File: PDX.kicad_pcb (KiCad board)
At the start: 2 copper layers, 97.3 x 97 mm, 104 parts, among them Q1 BS170, Q2 BS170, Q3 BS170, Q4 BS170, Q5 BC547, Q6 BC547, U1 CD2003GB_GP, U2 SI5351_Module, U3 74ACT244, U6 LM393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

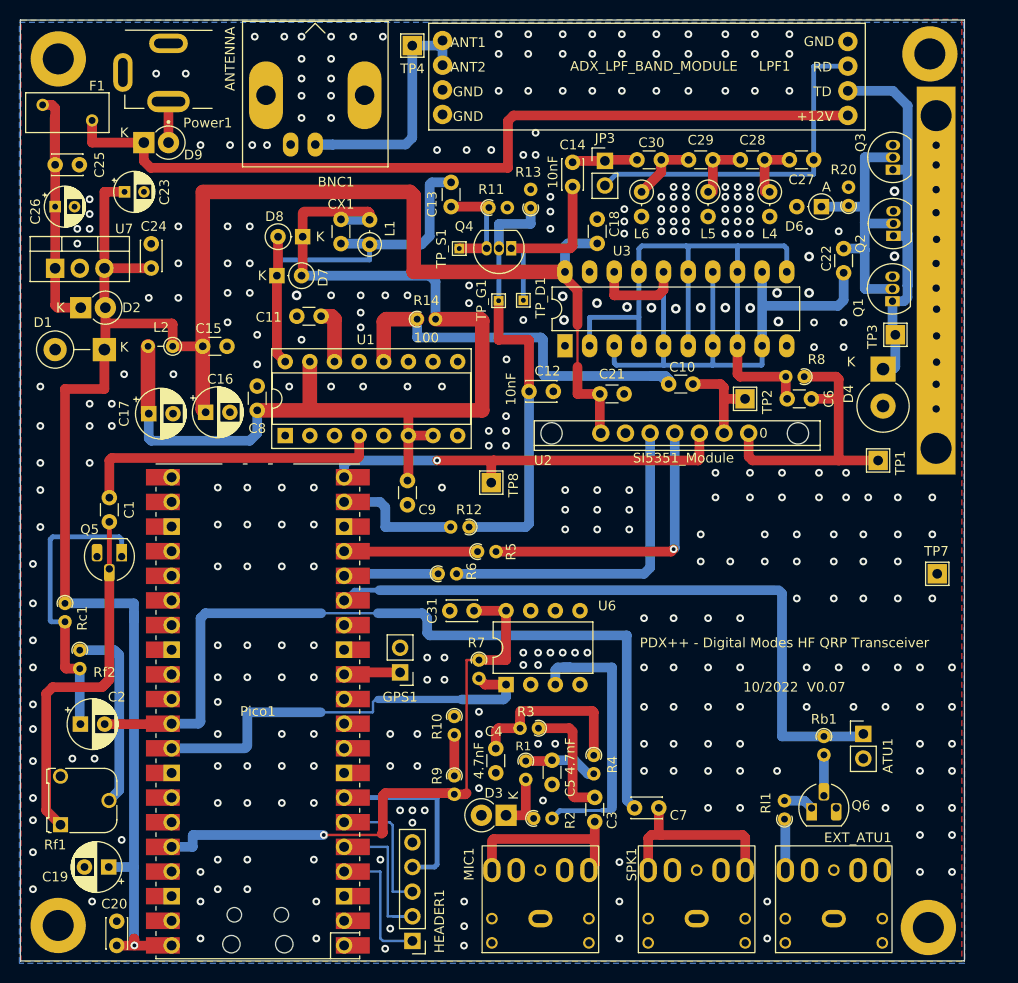
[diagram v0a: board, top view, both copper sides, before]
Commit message: PCB v0.2 + Initial firmware
PCB changes:

- Use `TO-92_HandSolder` footprint

- Use (optional) sockets for BS170 finals!

- Add `Test Point` for comparator output

- Remove onboard heatsink - it is not needed

- Provide +5V on the output header

- Make the +5V supply to Pico optional via a jumper

  - This enables external CAT control of Pico via USB

- Tie the unused LM393 inputs to ground

- Dual-input (+5V directly at VSYS and +5V from USB) power supply
  mechanism for Pico (similar to what Arduino Nano has).

Code changes:

- Initial firmware with CAT support (WSJT-X / 'FT8 Radio' Android app)

- The `freqPIO` stuff will be enabled later after testing
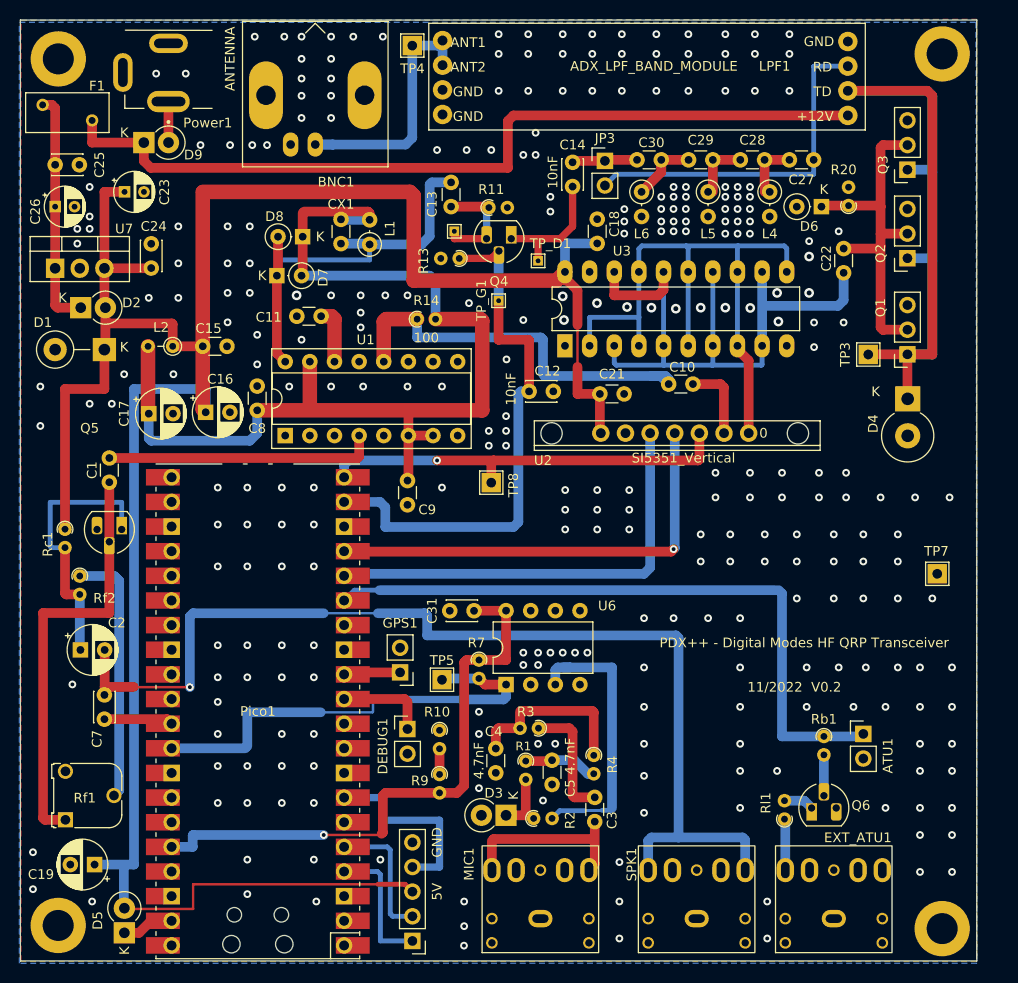
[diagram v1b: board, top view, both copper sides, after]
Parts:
- removed C20: 100nF, Capacitor_THT:C_Disc_D3.0mm_W2.0mm_P2.50mm
- removed C6: 100pF, Capacitor_THT:C_Disc_D3.0mm_W1.6mm_P2.50mm
- removed HS1: Heatsink_Pad, footprints:ThermalPad_Final
- removed R12, R5, R6: 330, Resistor_THT:R_Axial_DIN0204_L3.6mm_D1.6mm_P1.90mm_Vertical
- removed R8: 100, Resistor_THT:R_Axial_DIN0204_L3.6mm_D1.6mm_P1.90mm_Vertical
- removed TP1: CLK0, TestPoint:TestPoint_THTPad_2.0x2.0mm_Drill1.0mm
- removed TP2: CLK1, TestPoint:TestPoint_THTPad_2.0x2.0mm_Drill1.0mm
- added D5: 1N5818, Diode_THT:D_DO-41_SOD81_P2.54mm_Vertical_KathodeUp, F.Cu at (69.6, 106.9)
- added DEBUG1: Conn_01x02, Connector_PinHeader_2.54mm:PinHeader_1x02_P2.54mm_Vertical, F.Cu at (98.8, 85.9)
- added TP5: COUT, TestPoint:TestPoint_THTPad_2.0x2.0mm_Drill1.0mm, F.Cu at (102.4, 80.8)
- C26: value 100uF/16V -> 100uF/25V
- D6: footprint Diode_THT:D_DO-35_SOD27_P2.54mm_Vertical_AnodeUp -> Diode_THT:D_DO-35_SOD27_P2.54mm_Vertical_KathodeUp
- Q1, Q2, Q3: footprint Package_TO_SOT_THT:TO-92_Inline -> Connector_PinSocket_2.54mm:PinSocket_1x03_P2.54mm_Vertical
- Q4: footprint Package_TO_SOT_THT:TO-92_Inline -> Package_TO_SOT_THT:TO-92_HandSolder
- R20: value 2.7k -> 2.2k
- U2: value SI5351_Module -> SI5351_Vertical
- moved C7 57.9 mm to (67.6, 84.8), turned to 90 degrees
- moved R13 9.02 mm to (104.1, 37.3), turned to 180 degrees
- moved Rf2 7.65 mm to (65.0, 70.1)
- moved C2 7.64 mm to (65.1, 77.7)
- moved Rc1 7.64 mm to (63.5, 65.3)
- moved Q1 5.69 mm to (150.3, 47.2), turned to 180 degrees
- moved TP_D1 4.34 mm to (112.3, 37.6)
- moved C1 4.08 mm to (68.1, 57.9)
- moved D4 3.98 mm to (150.4, 51.8)
- moved TP3 3.45 mm to (146.3, 47.2)
- moved Q5 2.79 mm to (69.3, 65.3)
- moved Q2 2.73 mm to (150.3, 37.3), turned to 180 degrees
- moved R10 2.09 mm to (102.1, 86.0)
- moved TP_S1 1.85 mm to (103.6, 34.5), turned to 0 degrees
- moved R9 1.53 mm to (102.1, 90.5)
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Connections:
- C2 pad 2: TO_ADC -> Net-(C2-Pad2)
- C7 pad 1: Net-(C7-Pad1) -> TO_ADC
- C7 pad 2: TO_ADC -> Net-(C2-Pad2)
- HEADER1 pad 3: SW3 -> +5V
- Pico1 pad 11: unconnected-(Pico1-Pad11) -> Net-(DEBUG1-Pad1)
- Pico1 pad 19: Net-(Pico1-Pad19) -> RXSW
- Pico1 pad 39: unconnected-(Pico1-Pad39) -> Net-(D5-Pad1)
- Pico1 pad 40: +5V -> unconnected-(Pico1-Pad40)
- Pico1 pad 6: SW3 -> unconnected-(Pico1-Pad6)
- SPK1 pad R: Net-(C7-Pad1) -> Net-(C2-Pad2)
- SPK1 pad T: Net-(C7-Pad1) -> Net-(C2-Pad2)
- U2 pad 3: Net-(R6-Pad2) -> SDA
- U2 pad 4: Net-(R5-Pad2) -> SCL
- U2 pad 7: Net-(C6-Pad1) -> Net-(U2-Pad7)
- U3 pad 11: Net-(C6-Pad2) -> Net-(U2-Pad7)
- U3 pad 13: Net-(C6-Pad2) -> Net-(U2-Pad7)
- U3 pad 15: Net-(C6-Pad2) -> Net-(U2-Pad7)
- U3 pad 17: Net-(C6-Pad2) -> Net-(U2-Pad7)
- U3 pad 2: Net-(C6-Pad2) -> Net-(U2-Pad7)
- U3 pad 4: Net-(C6-Pad2) -> Net-(U2-Pad7)
- U3 pad 6: Net-(C6-Pad2) -> Net-(U2-Pad7)
- U3 pad 8: Net-(C6-Pad2) -> Net-(U2-Pad7)
- U6 pad 5: unconnected-(U6-Pad5) -> GNDPWR
- U6 pad 6: unconnected-(U6-Pad6) -> GNDPWR
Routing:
- net Net-(C2-Pad2): track 0.00 -> 110.4 mm, vias 0 -> 1
- net TO_ADC: track 84.7 -> 7.12 mm
- net Net-(C6-Pad2): track 66.7 -> 0.00 mm
- net Net-(U2-Pad7): track 0.00 -> 65.7 mm
- net TD_IN: track 44.6 -> 90.3 mm
- net SDA: track 9.48 -> 45.5 mm
- net Net-(R6-Pad2): track 34.1 -> 0.00 mm
- net SCL: track 13.7 -> 46.0 mm, vias 0 -> 1
- net Net-(C6-Pad1): track 30.9 -> 0.00 mm
- net Net-(R5-Pad2): track 30.4 -> 0.00 mm, vias 1 -> 0
- net Net-(C7-Pad1): track 19.8 -> 0.00 mm
- net SW3: track 14.0 -> 0.00 mm
- net Net-(Pico1-Pad19): track 13.2 -> 0.00 mm
- net Net-(DEBUG1-Pad1): track 0.00 -> 9.45 mm
- net Net-(C22-Pad1): track 28.9 -> 37.0 mm
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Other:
- board size 97.3 x 97 mm -> 98.6 x 97 mm
- board text added: "11/2022 V0.2"
- board text added: "5V"
- board text added: "GND"
- board text removed: "10/2022 V0.07"
